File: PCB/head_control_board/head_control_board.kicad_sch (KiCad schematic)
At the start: 24 parts, among them J1 Conn_01x02_Socket, U1 ESP32-S3-WROOM-1(N16R8), U2 CH9102F, U3 TPS63070RNMR

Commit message: Add MCU
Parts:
- removed D1: IP4234CZ6,125, :SOT-457_L2.9-W1.5-P0.95-LS2.8-BL, symbol LCSC:IP4234CZ6,125
- removed U2: CH9102F, :QFN-24_L4.0-W4.0-P0.50-BL-EP2.5, symbol LCSC:CH9102F
- removed USB1: TYPE-C 16PIN 2MD(073), :USB-C-SMD_TYPE-C-6PIN-2MD-073, symbol LCSC:TYPE-C16PIN2MD(073)
- added BOOT1, RESET1: TS-1187A-B-A-B, :SW-SMD_4P-L5.1-W5.1-P3.70-LS6.5-TL-2, symbol LCSC:TS-1187A-B-A-B
- added C10, C22: 100nF, symbol Device:C
- added C12, C14, C17: 22uF 0805, symbol Device:C
- added C15, C18: 10uF, symbol Device:C
- added C19, C20, C21: 0.1uF, symbol Device:C
- added C2, C4: 10uF 0805, symbol Device:C
- added C6, C8: 10uF 0603, symbol Device:C
- added D4, D5: D, symbol Device:D_Schottky
- added D6: IP4234CZ6,125, :SOT-457_L2.9-W1.5-P0.95-LS2.8-BL, symbol LCSC:IP4234CZ6,125
- added H1, H2: MountingHole_Pad, symbol Mechanical:MountingHole_Pad
- added HOLO1, LOGIC1, PSI1: JST-XH 3P, symbol Connector:Conn_01x03_Socket
- added L2: 1.5uH, symbol Device:L
- added LED1: WS2812B-MINI, :LED-SMD_4P-L3.5-W3.5-TL_WS2812B, symbol LCSC:WS2812B-MINI
- added R10: 100k, symbol Device:R
- added R11, R13, R4: 10k, symbol Device:R
- added R12: 60, symbol Device:R
- added R6: 470k, symbol Device:R
- added R8: 150k, symbol Device:R
- added RADAR1: JST-XH 2P, symbol Connector:Conn_01x02_Socket
- added U1: TYPE-C 14PLC-H10.0, :USB-C-TH_SHOUHAN_TYPE-C-14PLC-H10.0, symbol LCSC:TYPE-C14PLC-H10.0
- added U3: TPS63070RNMR, :VQFN-HR-15_L3.0-W2.5-P0.50-BL_TPS63070RNMR, symbol LCSC:TPS63070RNMR
- added U4: SN74AHCT245PWR, :TSSOP-20_L6.5-W4.4-P0.65-LS6.4-BL, symbol LCSC:SN74AHCT245PWR
- COIL1: renamed from J1; value Conn_01x02_Socket -> JST-XH 2P
- R5: value 523k -> 680k
- R7: renamed from R6; value 100k -> 130k
- renumbered C6 to C11, C7 to C13, C8 to C16, C2 to C3, C3 to C5, C5 to C7, C4 to C9, D3 to D1, D5 to D3, R4 to R9, U3 to U2, U1 to U5
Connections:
- net +5V: now also C15.2, HOLO1.1 (Pin_1), LOGIC1.1 (Pin_1), PSI1.1 (Pin_1), U4.1 (DIR), U4.20 (VCC)
- net +VCOIL: now also D2.2 (A)
- net +VUSB: now also D4.2 (A), D5.2 (A), U1.A4 (VBUS), U1.A9 (VBUS), U1.B4 (VBUS), U1.B9 (VBUS); no longer D2.2 (A)
- net GND: now also R1.1, R2.1, U5.1 (GND), U5.40 (GND), U5.41 (GND), BOOT1.4 (D), C10.2, C12.1, C14.1, C15.1, C17.1, C18.1, C19.1, C2.1, C20.1, C21.2, C22.1, C4.1, C6.1, C8.1, D6.2, H1.1, H2.1, HOLO1.3 (Pin_3), LED1.1 (VDD), LOGIC1.3 (Pin_3), PSI1.3 (Pin_3), R8.1, RADAR1.2 (Pin_2), RESET1.3 (C), U1.0, U1.A1 (GND), U1.A12 (GND), U1.B1 (GND), U1.B12 (GND), U3.10 (PGND), U3.15 (Vsel), U3.4 (GND), U3.6 (FB2), U4.10 (GND), U4.19 (~{OE}); no longer R1.2, R2.2
- net USB-D+: now also U5.14 (IO20), D6.4
- net USB-D-: now also U5.13 (IO19), D6.3
- net at D2.1 (K): now also C2.2, C4.2, C6.2, D4.1 (K), R4.1, U3.12 (Vin), U3.13 (Vin)
- net +3.3V: now reaches U5.2 (3V3)
- net +3.3V: now also C12.2, C14.2, C17.2, C18.2, C19.2, C22.2, C8.2, LED1.3 (VSS), R10.1, R11.1, R12.1, R13.2, R6.2, U3.7 (Vout), U3.8 (Vout)
- net at U5.27 (IO0): now also BOOT1.1 (A), C21.1
- net at U5.3 (EN): now also C20.2, RESET1.2 (B)
- net LED3_3V3: now reaches U5.33 (IO40)
- net LED3_3V3: now also U4.4 (A3)
- net LED2_3V3: now reaches U5.34 (IO41)
- net LED2_3V3: now also U4.3 (A2)
- net LED1_3V3: now reaches U5.35 (IO42)
- net LED1_3V3: now also U4.2 (A1)
- net at U5.39 (IO1): now also LED1.4 (DIN)
- new net: R11.2, RESET1.1 (A)
- new net: D6.1, U1.A7 (D-), U1.B7 (D-)
- new net: D5.1 (K), D6.5
- new net: D6.6, U1.A6 (D+), U1.B6 (D+)
- new net: L2.1, U3.11 (L1)
- new net: L2.2, U3.9 (L2)
- new net: R12.2, RADAR1.1 (Pin_1)
- new net: BOOT1.2 (B), R13.1
- new net: R4.2, U3.1 (PS/SYNC), U3.14 (EN)
- new net: R1.2, U1.A5 (CC1)
- new net: R6.1, R8.2, U3.5 (FB)
- new net: R10.2, U3.2 (PG)
- new net: R2.2, U1.B5 (CC2)
- new net: C10.1, U3.3 (Vaux)
- new net LED1_5V: HOLO1.2 (Pin_2), U4.18 (B1)
- new net LED2_5V: PSI1.2 (Pin_2), U4.17 (B2)
- new net LED3_5V: LOGIC1.2 (Pin_2), U4.16 (B3)
- no-connect marks 2 -> 42
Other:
- moved on the sheet: C1, C11, C13, C16, C3, C5, C7, C9, D1, D3, L1, R3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

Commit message: Finish first pass of schematic
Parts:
- added TP1, TP2: TestPoint, TestPoint:TestPoint_Pad_D2.0mm, symbol Connector:TestPoint
- BOOT1, RESET1: footprint :SW-SMD_4P-L5.1-W5.1-P3.70-LS6.5-TL-2 -> LCSC:SW-SMD_4P-L5.1-W5.1-P3.70-LS6.5-TL-2
- C1, C11, C12, C13, C14, C15, C16, C17, C18, C2, C3, C4: footprint (none) -> Capacitor_SMD:C_0805_2012Metric
- C10, C22, C9: footprint (none) -> Capacitor_SMD:C_0402_1005Metric
- C19, C20, C21, C5, C6, C7, C8: footprint (none) -> Capacitor_SMD:C_0603_1608Metric
- COIL1, RADAR1: footprint (none) -> Connector_JST:JST_XH_S2B-XH-A-1_1x02_P2.50mm_Horizontal
- D1, D2, D3, D4, D5: footprint (none) -> :SMA_L4.3-W2.6-LS5.2-RD; symbol Device:D_Schottky -> LCSC:SS34_C8678; LCSC Part (none) -> C8678
- D6: footprint :SOT-457_L2.9-W1.5-P0.95-LS2.8-BL -> LCSC:SOT-457_L2.9-W1.5-P0.95-LS2.8-BL
- H1, H2: footprint (none) -> MountingHole:MountingHole_2.5mm_Pad_Via
- HOLO1, LOGIC1, PSI1: footprint (none) -> Connector_JST:JST_XH_S3B-XH-A-1_1x03_P2.50mm_Horizontal
- L1, L2: footprint (none) -> LCSC:IND-SMD_L7.0-W6.6
- LED1: footprint :LED-SMD_4P-L3.5-W3.5-TL_WS2812B -> LCSC:LED-SMD_4P-L3.5-W3.5-TL_WS2812B
- R1, R11, R12, R13, R2, R3, R4: footprint (none) -> Resistor_SMD:R_0805_2012Metric
- R10, R5, R6, R7, R8, R9: footprint (none) -> Resistor_SMD:R_0603_1608Metric
- U1: footprint :USB-C-TH_SHOUHAN_TYPE-C-14PLC-H10.0 -> LCSC:USB-C-TH_SHOUHAN_TYPE-C-14PLC-H10.0
- U2, U3: footprint :VQFN-HR-15_L3.0-W2.5-P0.50-BL_TPS63070RNMR -> LCSC:VQFN-HR-15_L3.0-W2.5-P0.50-BL_TPS63070RNMR
- U4: footprint :TSSOP-20_L6.5-W4.4-P0.65-LS6.4-BL -> LCSC:TSSOP-20_L6.5-W4.4-P0.65-LS6.4-BL
- U5: footprint :WIRELM-SMD_ESP32-S3-WROOM-1 -> LCSC:WIRELM-SMD_ESP32-S3-WROOM-1
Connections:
- net +3.3V: now also TP2.1
- net +5V: now also TP1.1
- net LED1_3V3: now also U5.19 (IO11); no longer U5.35 (IO42)
- net LED2_3V3: now also U5.20 (IO12); no longer U5.34 (IO41)
- net LED3_3V3: now also U5.21 (IO13); no longer U5.33 (IO40)
- net USB-D+: now also D6.3; no longer D6.4
- net USB-D-: now also D6.4; no longer D6.3
- net D-: now reaches U1.A7 (D-), U1.B7 (D-)
- net D-: now also D6.6; no longer D6.1
- net D+: now reaches U1.A6 (D+), U1.B6 (D+)
- net D+: now also D6.1; no longer D6.6
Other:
- moved on the sheet: BOOT1, C18, C19, C20, C21, C22, COIL1, H1, H2, HOLO1, LED1, LOGIC1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

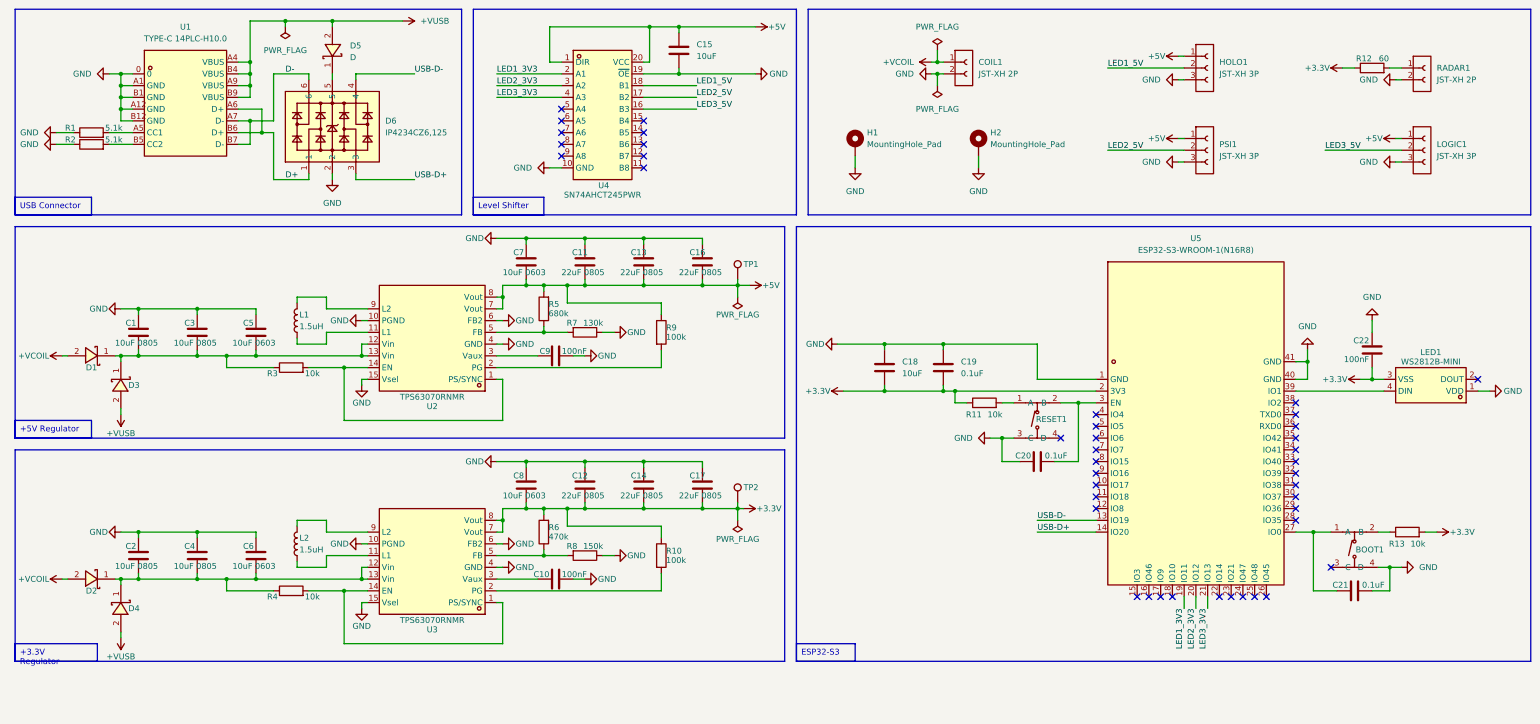
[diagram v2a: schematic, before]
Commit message: Update schematic and route usb
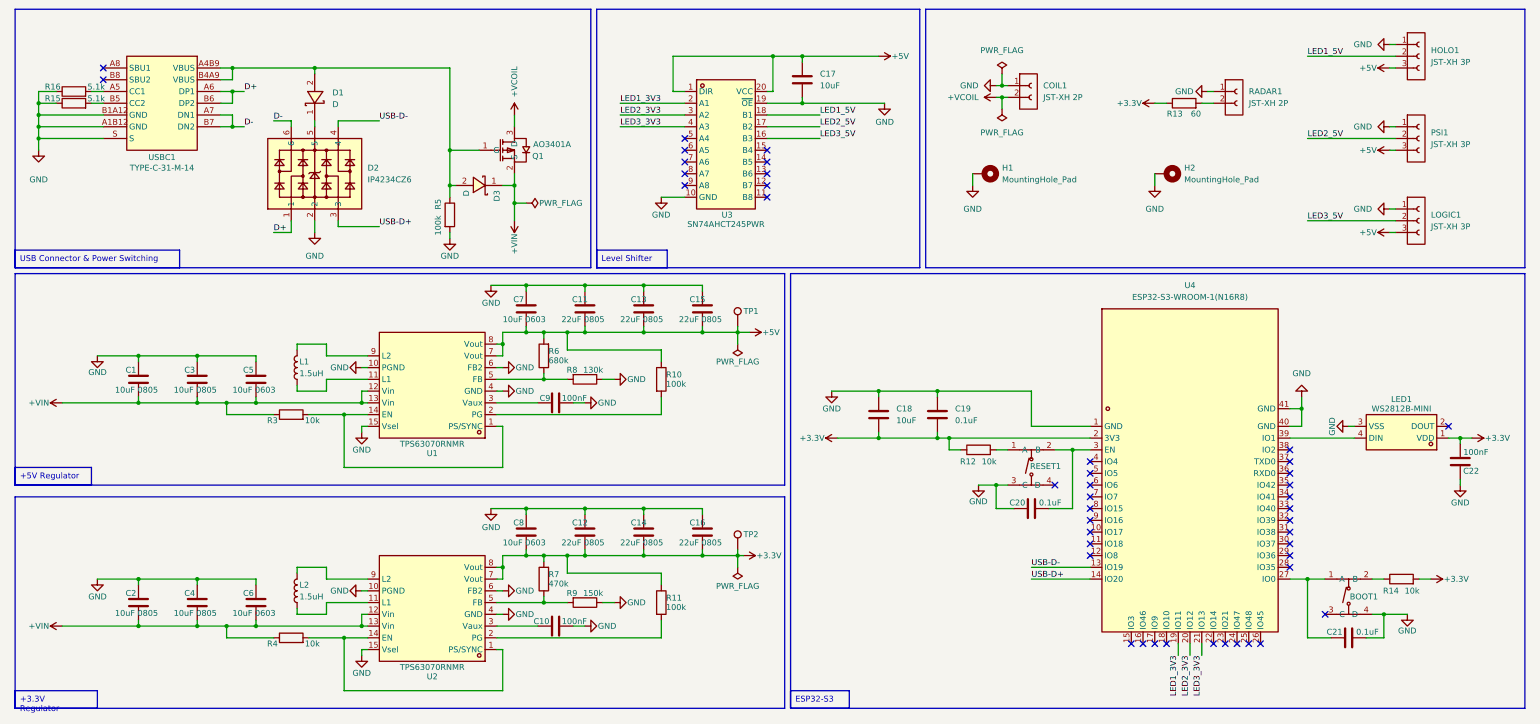
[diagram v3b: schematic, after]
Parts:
- removed D2, D4, D5: D, :SMA_L4.3-W2.6-LS5.2-RD, symbol LCSC:SS34_C8678
- removed D6: IP4234CZ6,125, LCSC:SOT-457_L2.9-W1.5-P0.95-LS2.8-BL, symbol LCSC:IP4234CZ6,125
- removed R1, R2: 5.1k, Resistor_SMD:R_0805_2012Metric, symbol Device:R
- removed U1: TYPE-C 14PLC-H10.0, LCSC:USB-C-TH_SHOUHAN_TYPE-C-14PLC-H10.0, symbol LCSC:TYPE-C14PLC-H10.0
- added D2: IP4234CZ6, LCSC:SOT-457_L2.9-W1.5-P0.95-LS2.8-BL, symbol LCSC:IP4234CZ6,125
- added Q1: AO3401A, LCSC:SOT-23_L2.9-W1.3-P1.90-LS2.4-BR, symbol LCSC:AO3401A
- added R15, R16: 5.1k, Resistor_SMD:R_0805_2012Metric, symbol Device:R
- added R5: 100k, Resistor_SMD:R_0805_2012Metric, symbol Device:R
- added USBC1: TYPE-C-31-M-14, :USB-C-SMD_12P-P0.50-H-F_TYPE-C-31-M-14, symbol LCSC:TYPE-C-31-M-14
- D1, D3: footprint :SMA_L4.3-W2.6-LS5.2-RD -> LCSC:SMA_L4.3-W2.6-LS5.2-RD
- renumbered C16 to C15, C17 to C16, C15 to C17, R9 to R10, R10 to R11, R11 to R12, R12 to R13, R13 to R14, R5 to R6, R6 to R7, R7 to R8, R8 to R9, U2 to U1, U3 to U2, U4 to U3, U5 to U4
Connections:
- net +3.3V: now also LED1.1 (VDD); no longer LED1.3 (VSS)
- net +5V: now also HOLO1.3 (Pin_3), LOGIC1.3 (Pin_3), PSI1.3 (Pin_3); no longer HOLO1.1 (Pin_1), LOGIC1.1 (Pin_1), PSI1.1 (Pin_1)
- net +VCOIL: now also COIL1.2 (Pin_2), Q1.3 (D); no longer COIL1.1 (Pin_1), D1.2
- net D+: now also D2.1, USBC1.A6 (DP1), USBC1.B6 (DP2)
- net D-: now also D2.6, USBC1.A7 (DN1), USBC1.B7 (DN2)
- net GND: now also COIL1.1 (Pin_1), HOLO1.1 (Pin_1), LED1.3 (VSS), LOGIC1.1 (Pin_1), PSI1.1 (Pin_1), RADAR1.1 (Pin_1), D2.2, R15.1, R16.1, R5.2, USBC1.A1B12 (GND), USBC1.B1A12 (GND), USBC1.S; no longer COIL1.2 (Pin_2), HOLO1.3 (Pin_3), LED1.1 (VDD), LOGIC1.3 (Pin_3), PSI1.3 (Pin_3), RADAR1.2 (Pin_2)
- net USB-D+: now also D2.3
- net USB-D-: now also D2.4
- net +VIN: now reaches C2.2, C4.2, C6.2, R4.1, U2.12 (Vin), U2.13 (Vin)
- net +VIN: now also C1.2, C3.2, C5.2, D3.1, R3.1, U1.12 (Vin), U1.13 (Vin), Q1.2 (S)
- net at R13.2: now also RADAR1.2 (Pin_2); no longer RADAR1.1 (Pin_1)
- net +VUSB: no longer names the net of D3.2
- net +VUSB: now also D1.2, Q1.1 (G), R5.1, USBC1.A4B9 (VBUS), USBC1.B4A9 (VBUS)
- new net: R15.2, USBC1.B5 (CC2)
- new net: D1.1, D2.5
- new net: R16.2, USBC1.A5 (CC1)
- no-connect marks 42 -> 44
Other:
- moved on the sheet: BOOT1, C1, C10, C11, C12, C13, C14, C15, C16, C17, C18, C19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

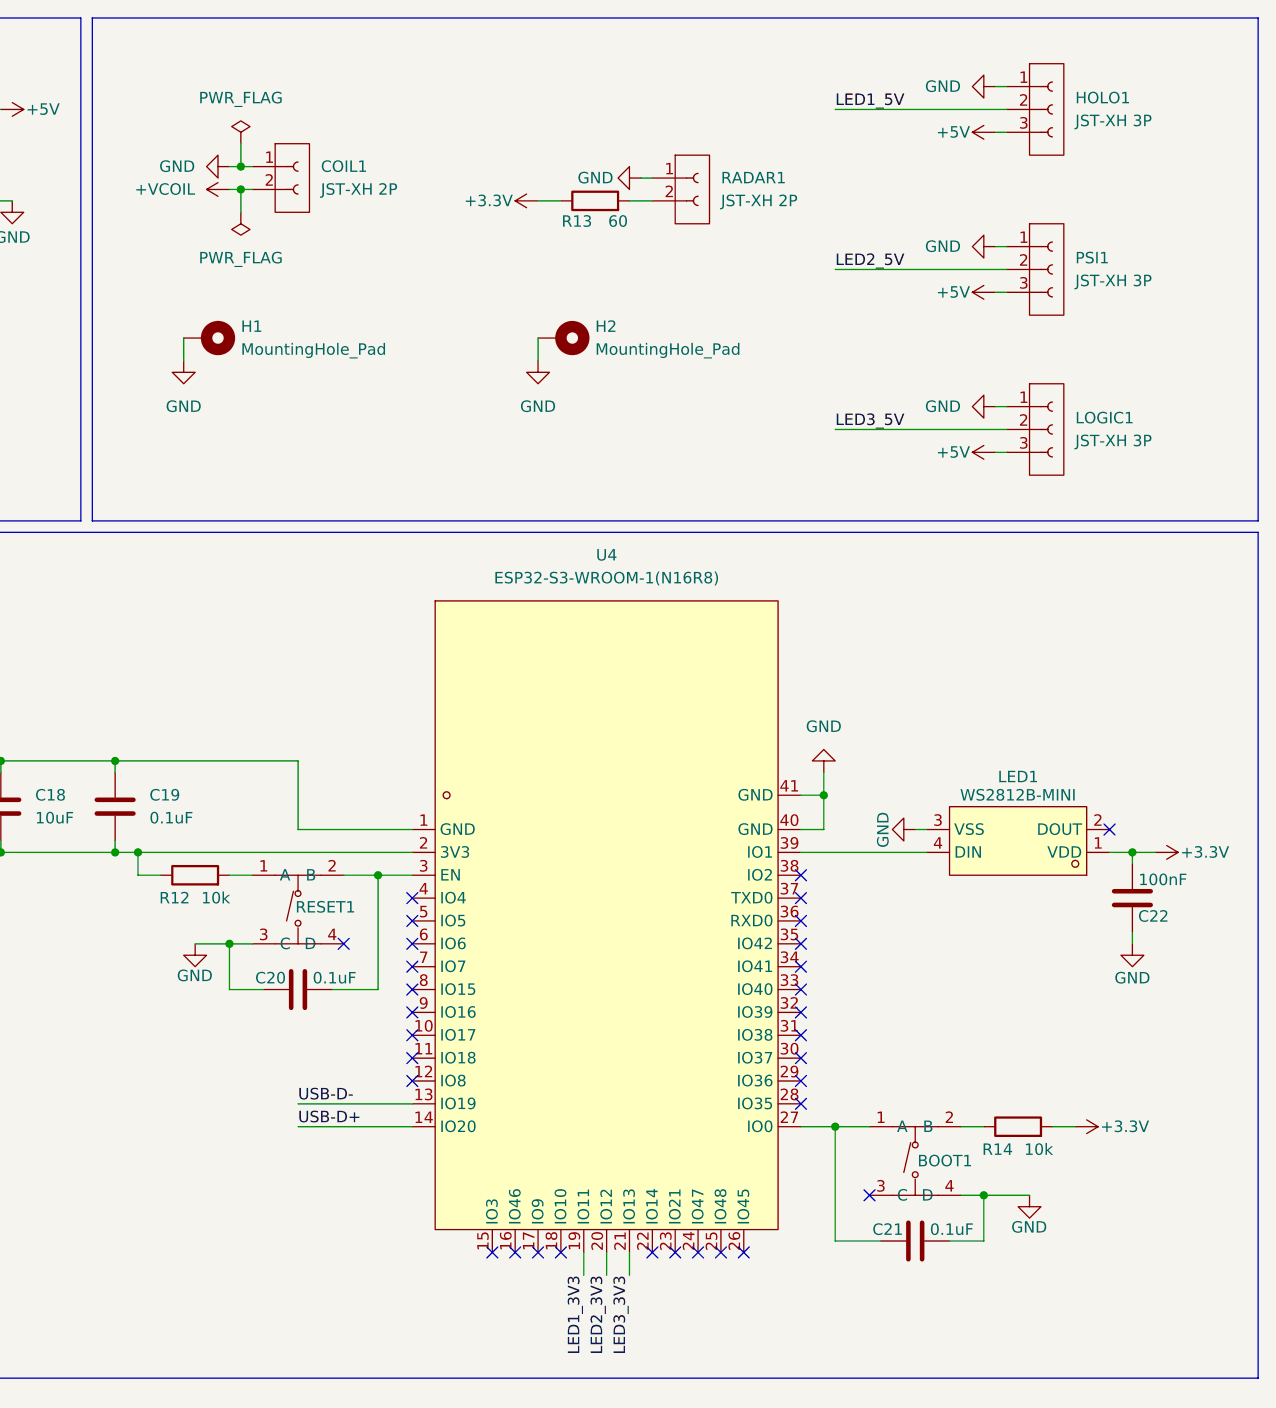
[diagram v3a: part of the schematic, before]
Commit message: First pass on voltage regulators
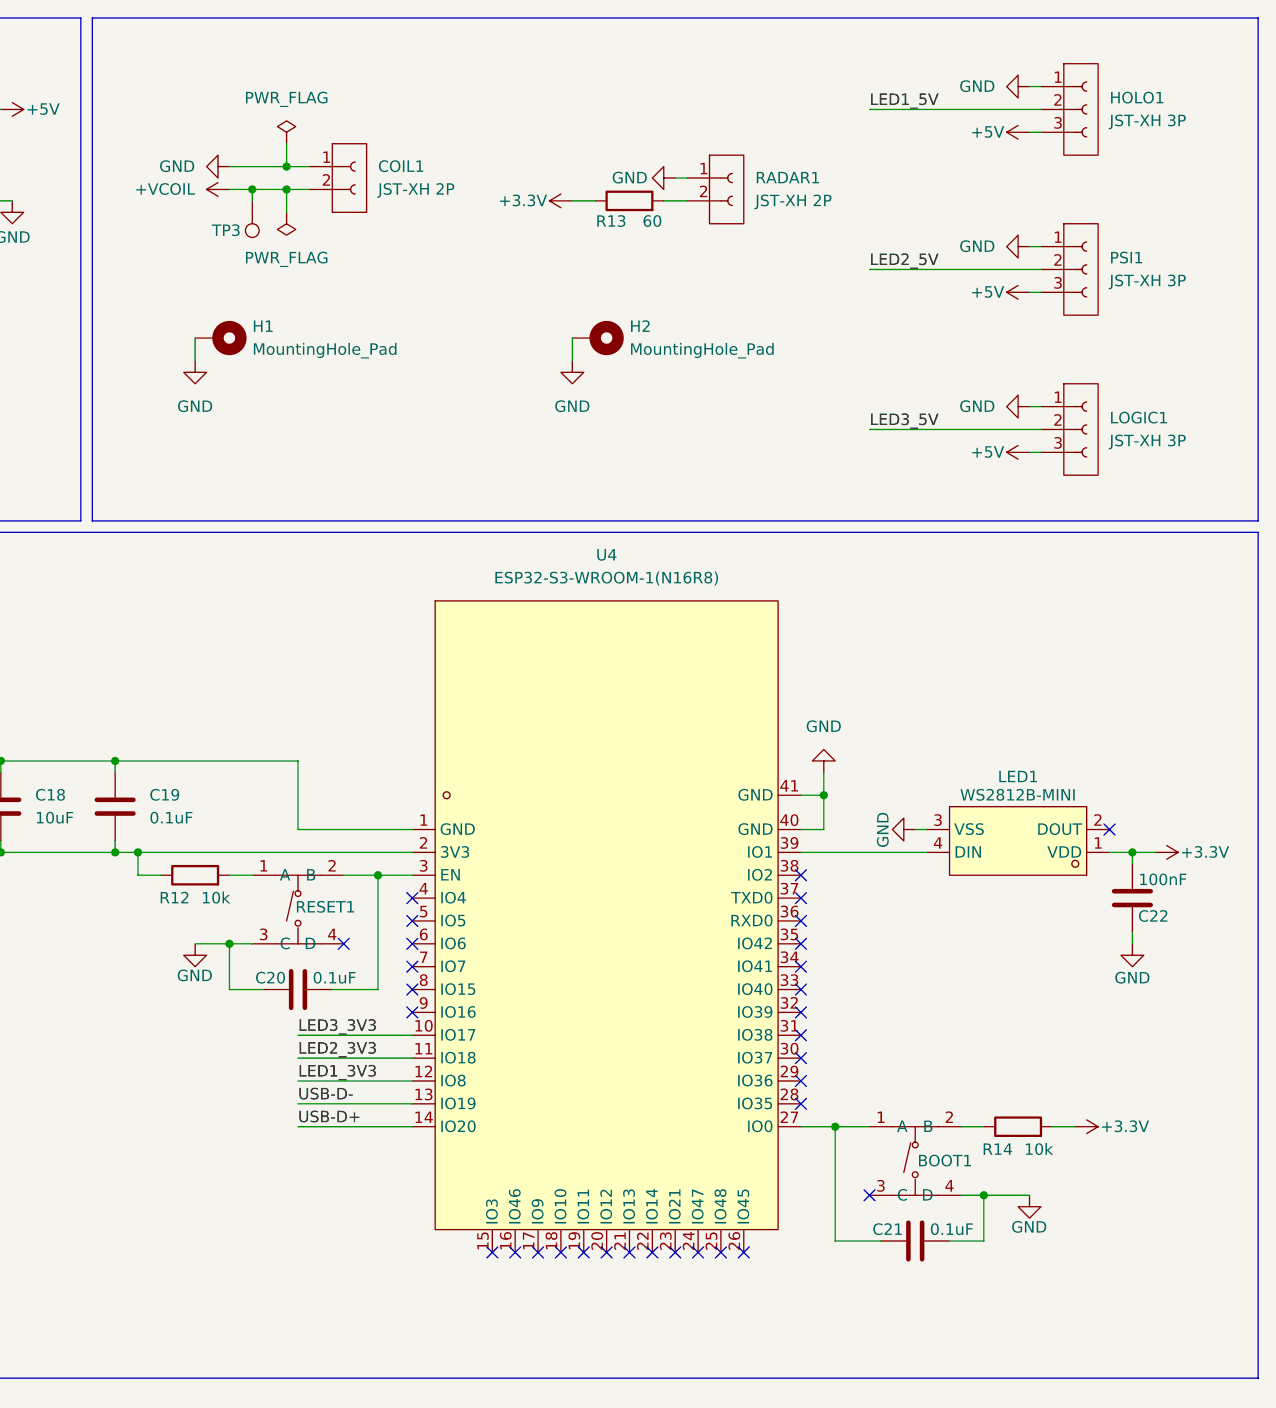
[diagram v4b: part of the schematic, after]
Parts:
- added TP3: TestPoint, TestPoint:TestPoint_Pad_D2.0mm, symbol Connector:TestPoint
- R10, R11, R6, R7, R8, R9: footprint Resistor_SMD:R_0603_1608Metric -> Resistor_SMD:R_0402_1005Metric
- R3, R4: footprint Resistor_SMD:R_0805_2012Metric -> Resistor_SMD:R_0402_1005Metric
- USBC1: footprint :USB-C-SMD_12P-P0.50-H-F_TYPE-C-31-M-14 -> LCSC:USB-C-SMD_12P-P0.50-H-F_TYPE-C-31-M-14
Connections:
- net +VCOIL: now also TP3.1
- net LED1_3V3: now also U4.12 (IO8); no longer U4.19 (IO11)
- net LED2_3V3: now also U4.11 (IO18); no longer U4.20 (IO12)
- net LED3_3V3: now also U4.10 (IO17); no longer U4.21 (IO13)
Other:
- moved on the sheet: COIL1, H1, H2, HOLO1, LOGIC1, PSI1, R13, RADAR1
